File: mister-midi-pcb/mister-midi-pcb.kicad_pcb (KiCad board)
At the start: 2 copper layers, 106.9 x 68.6 mm, 33 parts, among them J1 Midi In, J2 USB3_A, J3 Midi Out, J4 Midi Thru, U1 H11L1, U2 74HC14, U3 LM1117-3.3

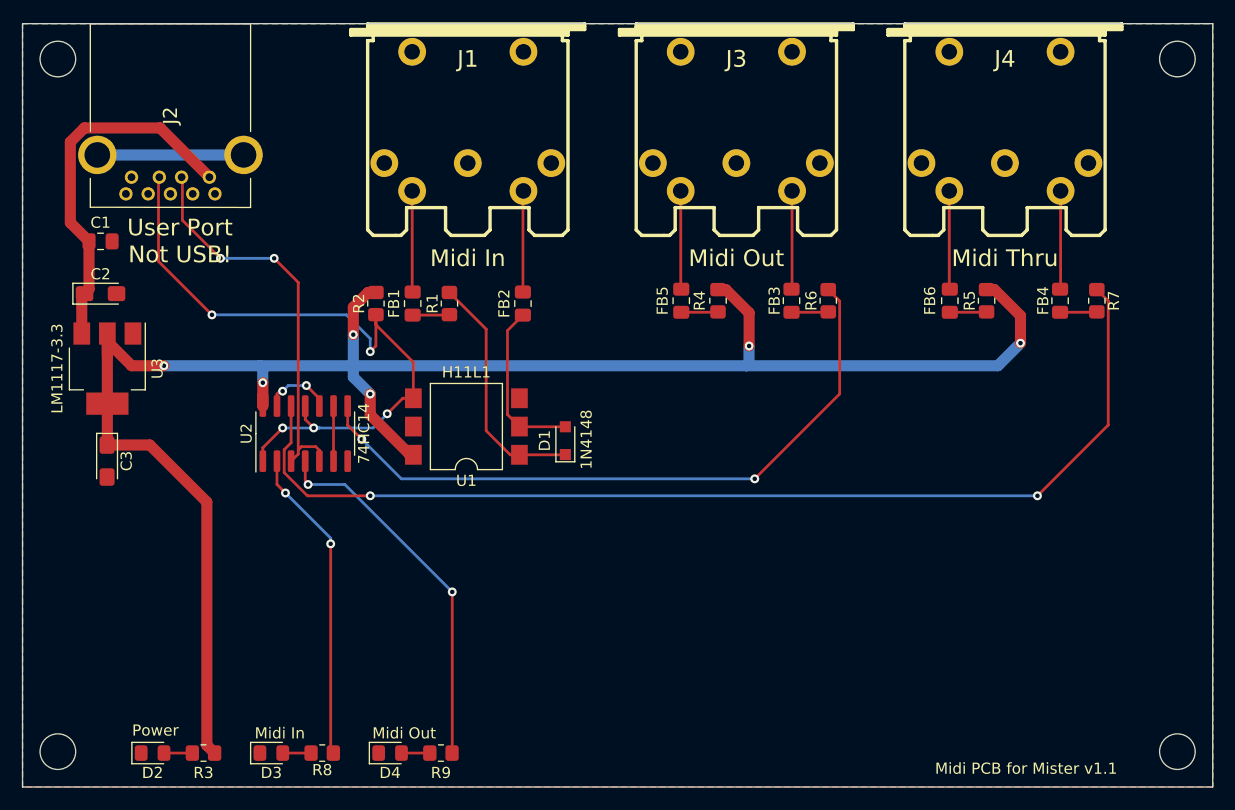
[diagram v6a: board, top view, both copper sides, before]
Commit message: kicad 6 migration, jlcpcb assembly files.
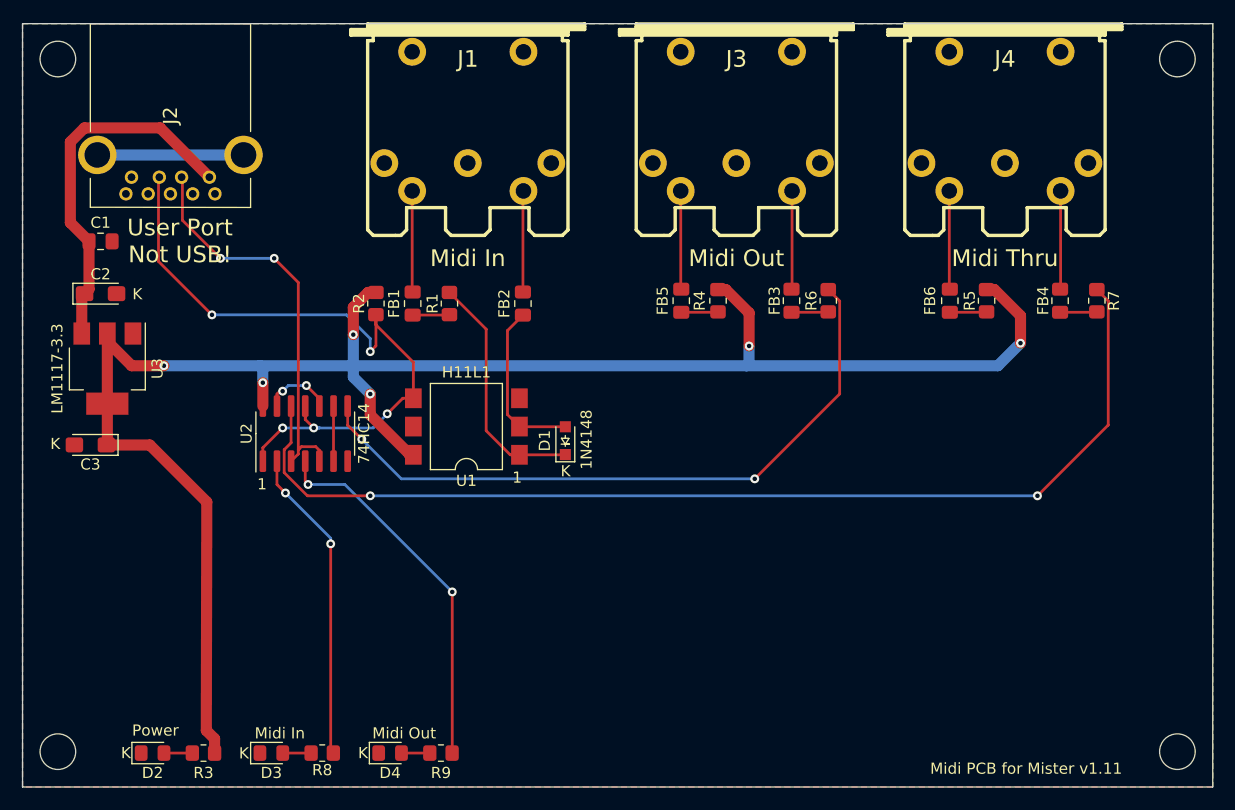
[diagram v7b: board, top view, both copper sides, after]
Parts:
- D4: value White LED -> Yellow LED
- moved C3 2.08 mm to (67.1, 114.0), turned to 180 degrees
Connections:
- J1 pad 1: Net-(J1-Pad1) -> unconnected-(J1-Pad1)
- J1 pad 2: Net-(J1-Pad2) -> unconnected-(J1-Pad2)
- J1 pad 3: Net-(J1-Pad3) -> unconnected-(J1-Pad3)
- J2 pad 10: Net-(J2-Pad10) -> unconnected-(J2-Pad10)
- J2 pad 5: Net-(J2-Pad5) -> unconnected-(J2-Pad5)
- J2 pad 6: Net-(J2-Pad6) -> unconnected-(J2-Pad6)
- J2 pad 7: Net-(J2-Pad7) -> unconnected-(J2-Pad7)
- J2 pad 8: Net-(J2-Pad8) -> unconnected-(J2-Pad8)
- J2 pad 9: Net-(J2-Pad9) -> unconnected-(J2-Pad9)
- J3 pad 1: Net-(J3-Pad1) -> unconnected-(J3-Pad1)
- J3 pad 3: Net-(J3-Pad3) -> unconnected-(J3-Pad3)
- J4 pad 1: Net-(J4-Pad1) -> unconnected-(J4-Pad1)
- J4 pad 3: Net-(J4-Pad3) -> unconnected-(J4-Pad3)
- U1 pad 3: Net-(U1-Pad3) -> unconnected-(U1-Pad3)
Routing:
- net unconnected-(J2-Pad10): track 0.00 -> 13.1 mm
- net Net-(J2-Pad10): track 13.1 -> 0.00 mm
- net +3V3: track 168.8 -> 165.8 mm
- net Net-(U2-Pad6): track 5.92 -> 4.95 mm
- net Net-(U2-Pad10): track 7.19 -> 6.36 mm
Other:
- net class 3.3V / 5V removed
- net class Default removed
- board text added: "1"
- board text added: "K"
- board text added: "Midi PCB for Mister v1.11"
- board text removed: "Midi PCB for Mister v1.1"
